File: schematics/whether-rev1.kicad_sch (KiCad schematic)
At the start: 3 parts, among them J1 Raspberry Pi Model 3B+, U1 DHT22

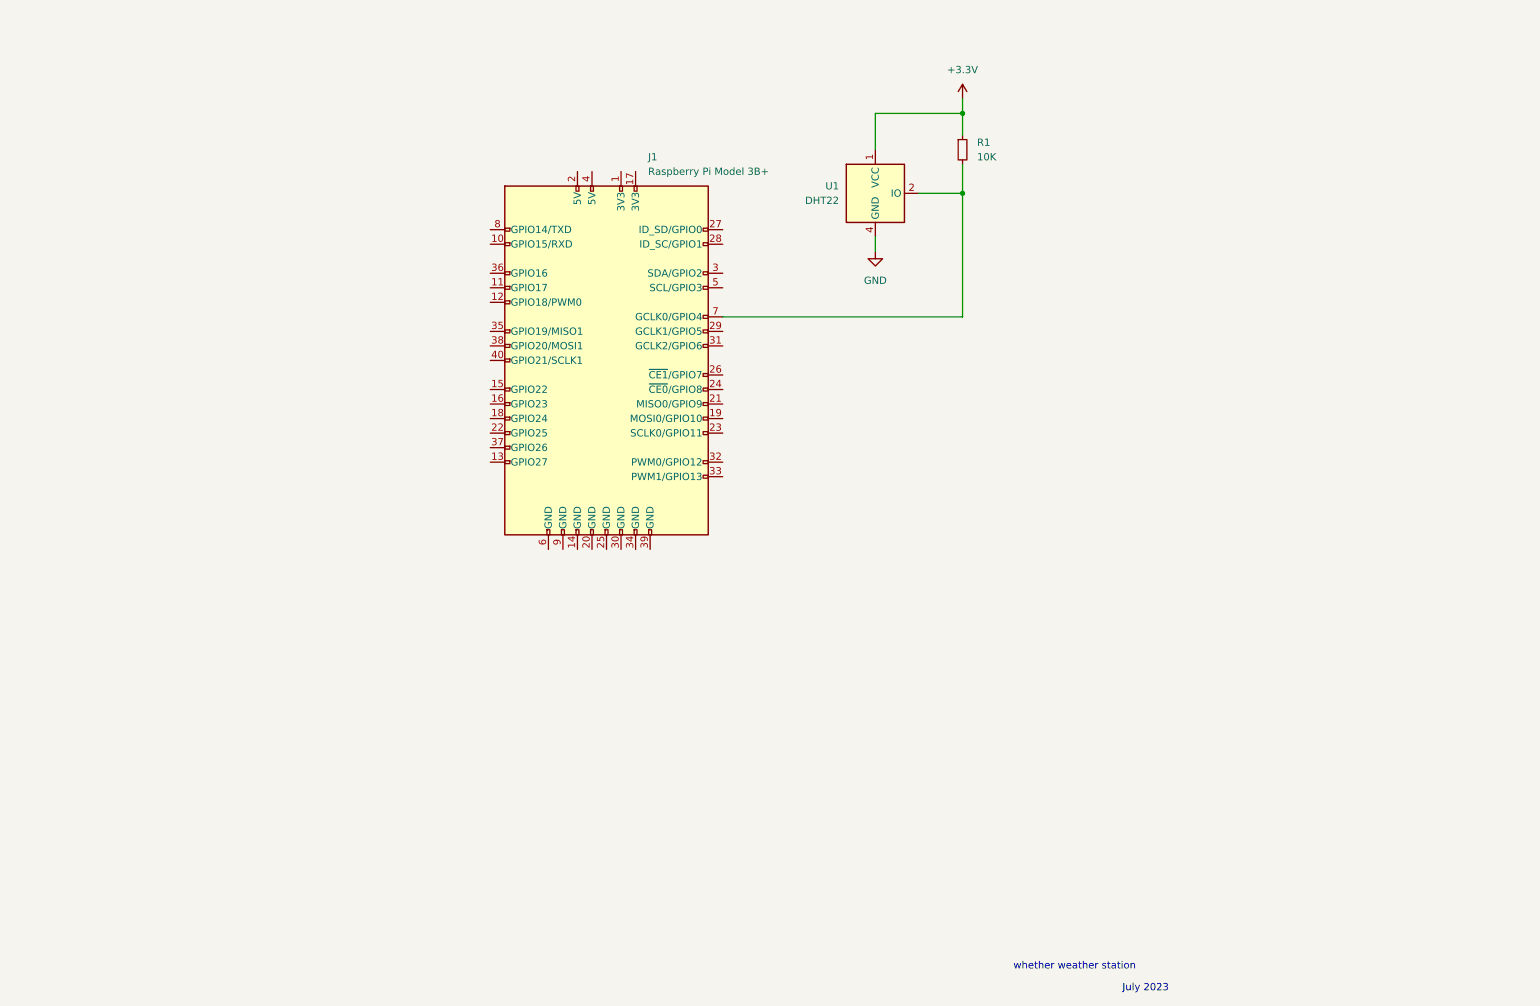
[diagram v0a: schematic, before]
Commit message: Added weather direction A-to-D
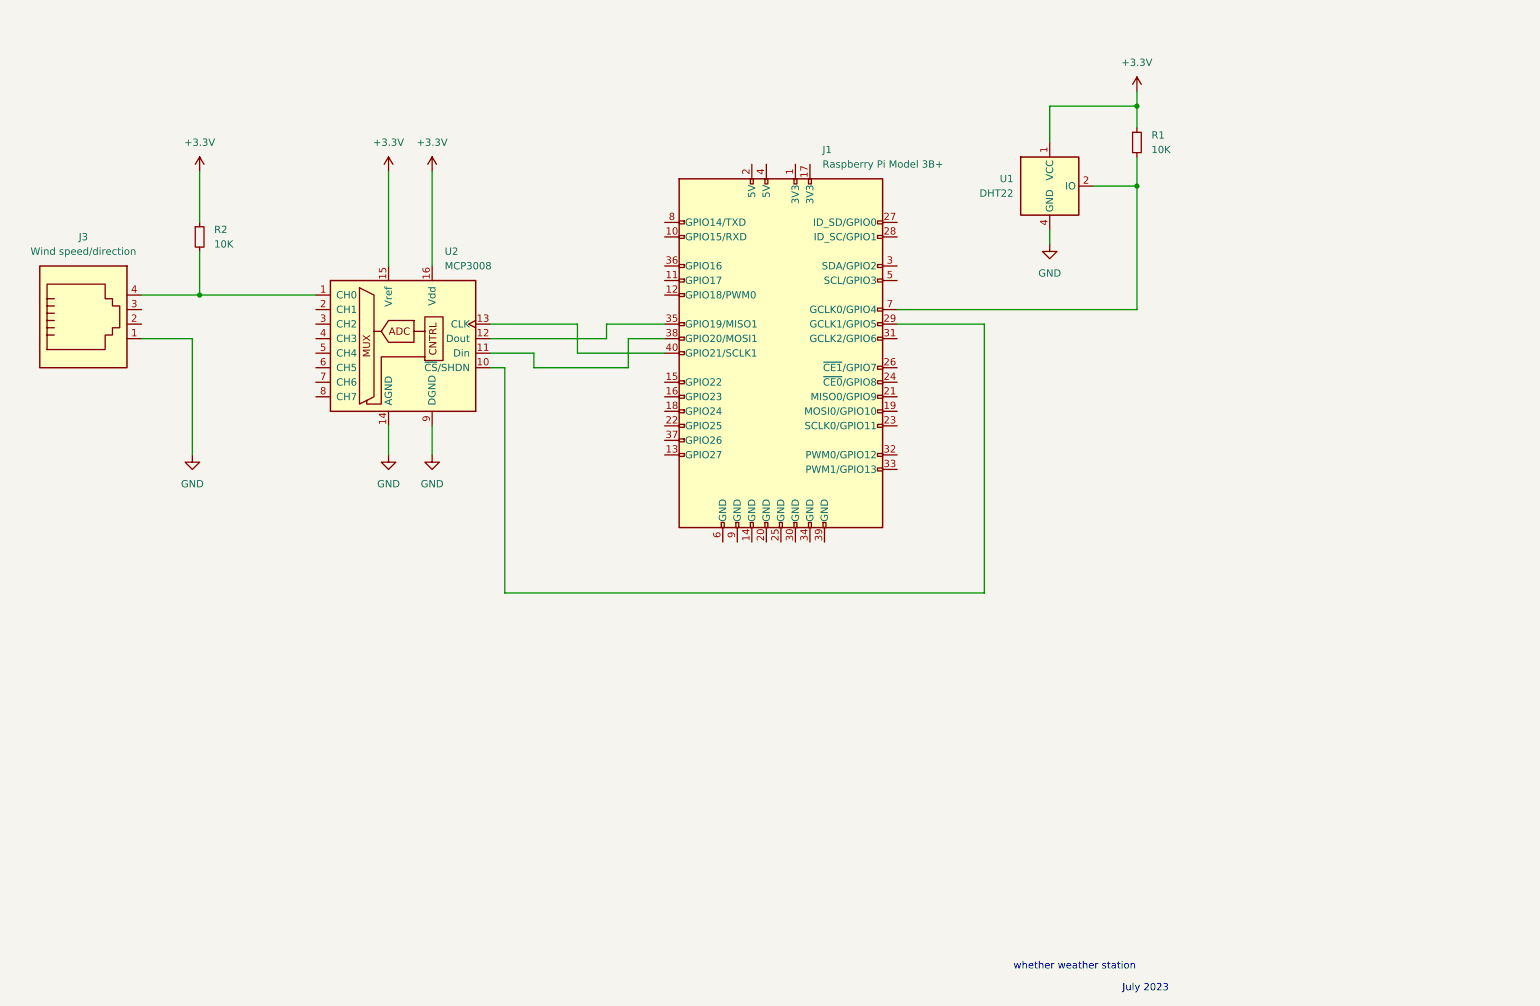
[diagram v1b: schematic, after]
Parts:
- added J3: Wind speed/direction, symbol Connector:6P4C
- added R2: 10K, symbol Device:R_Small
- added U2: MCP3008, symbol Analog_ADC:MCP3008
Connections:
- net +3.3V: now also R2.1, U2.15 (Vref), U2.16 (Vdd)
- net GND: now also J3.1, U2.14 (AGND), U2.9 (DGND)
- net at J1.29 (GCLK1/GPIO5): now also U2.10 (~{CS}/SHDN)
- net at J1.35 (GPIO19/MISO1): now also U2.12 (Dout)
- net at J1.38 (GPIO20/MOSI1): now also U2.11 (Din)
- net at J1.40 (GPIO21/SCLK1): now also U2.13 (CLK)
- new net: J3.4, R2.2, U2.1 (CH0)
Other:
- moved on the sheet: J1, R1, U1

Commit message: Added rain gauge circuit
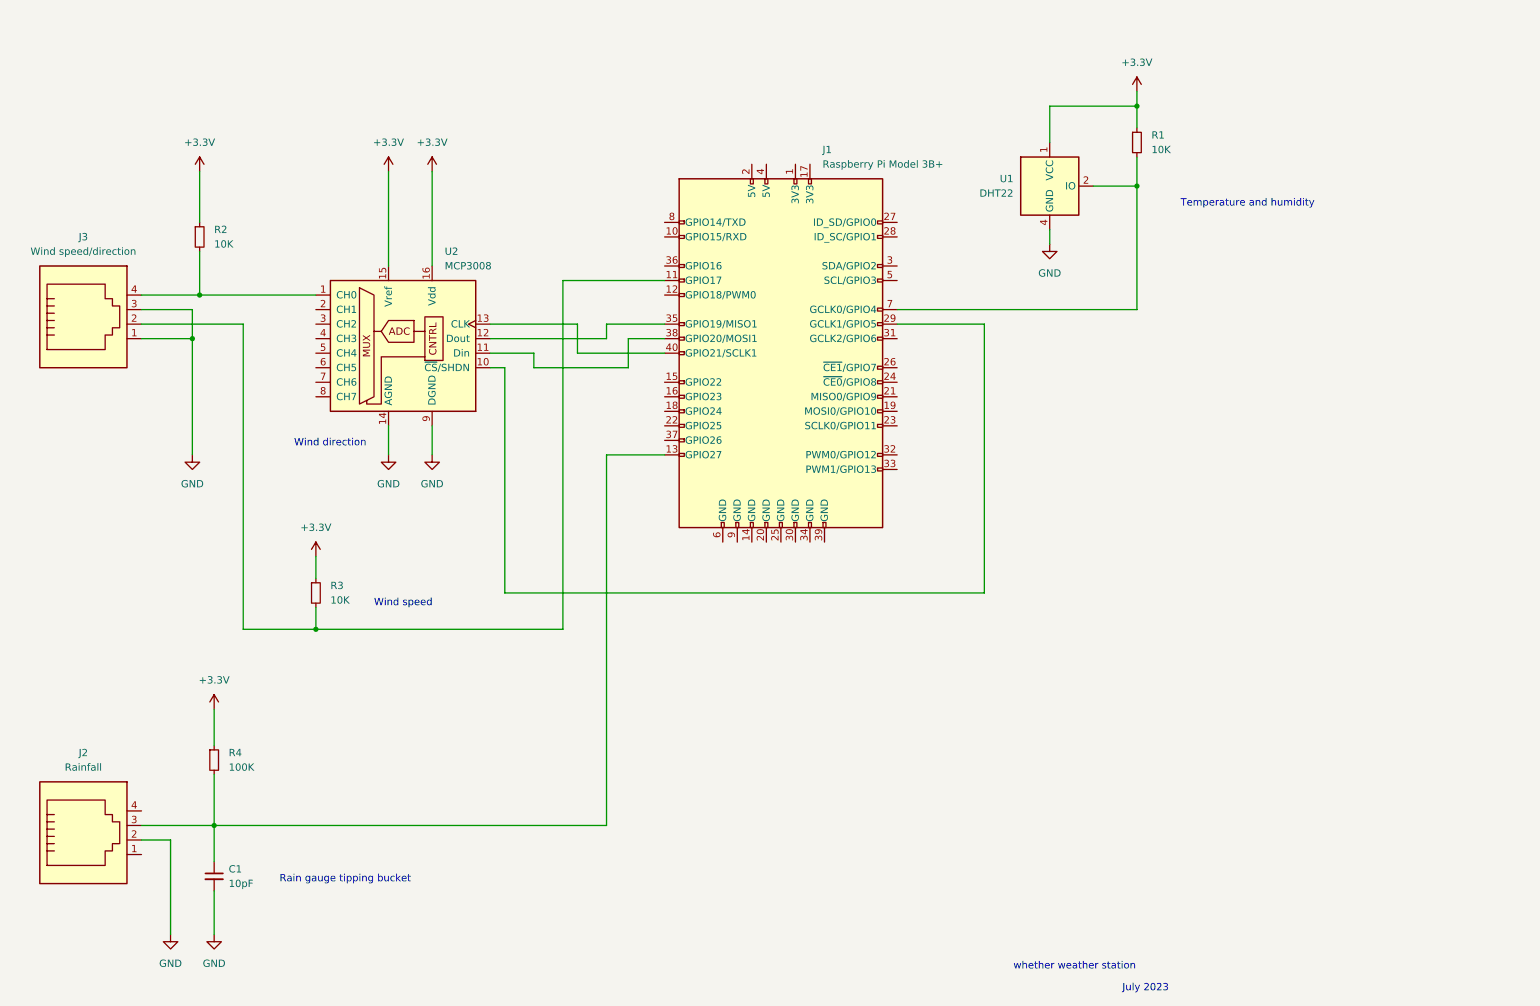
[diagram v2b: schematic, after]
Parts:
- added C1: 10pF, symbol Device:C_Small
- added J2: Rainfall, symbol Connector:6P4C
- added R3: 10K, symbol Device:R_Small
- added R4: 100K, symbol Device:R_Small
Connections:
- net +3.3V: now also R3.1, R4.1
- net GND: now also J3.3, C1.2, J2.2
- net at J1.11 (GPIO17): now also J3.2, R3.2
- net at J1.13 (GPIO27): now also C1.1, J2.3, R4.2
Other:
- note added: "Rain gauge tipping bucket"
- note added: "Temperature and humidity"
- note added: "Wind direction"
- note added: "Wind speed"

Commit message: Schematic for revision 1
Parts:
- R2: value 10K -> 5K6
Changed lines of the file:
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@@
       (effects (font (size 1.27 1.27)) (justify left))
     )
-    (property "Value" "10K" (at 49.53 63.5 0)
+    (property "Value" "5K6" (at 49.53 63.5 0)
       (effects (font (size 1.27 1.27)) (justify left))
     )

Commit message: Updated diagram
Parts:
- added C2: 10pF, symbol Device:C_Small
- R3: value 10K -> 680
- R4: value 100K -> 680
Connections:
- net GND: now also C2.2
- net at J1.11 (GPIO17), J3.2, R3.2: now also C2.1
- net at J1.19 (MOSI0/GPIO10): now also U2.11 (Din)
- net at J1.21 (MISO0/GPIO9): now also U2.12 (Dout)
- net at J1.23 (SCLK0/GPIO11): now also U2.13 (CLK)
- net at J1.35 (GPIO19/MISO1): no longer U2.12 (Dout)
- net at J1.38 (GPIO20/MOSI1): no longer U2.11 (Din)
- net at J1.40 (GPIO21/SCLK1): no longer U2.13 (CLK)
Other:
- moved on the sheet: J1, J3, R1, R2, R3, U1, U2
